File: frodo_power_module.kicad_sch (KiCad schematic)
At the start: 75 parts, among them J1 Keystone 1098, J10 SWD Header, J2 Molex MicroFit 2x2, J3 Molex MicroFit 2x2, J4 Molex MicroFit 2x2, J5 Molex MicroFit 2x2, J6 Molex MicroFit 2x2, J7 JST-GH, J8 JST-GH, J9 JST-GH, U1 STM32F042F6Px, U2 L7805, U3 AZ1117I-3.3, U4 BQ25171-Q1, U5 BQ29200, U6 MCP2562-E-SN, U7 INA213, Y1 8MHz

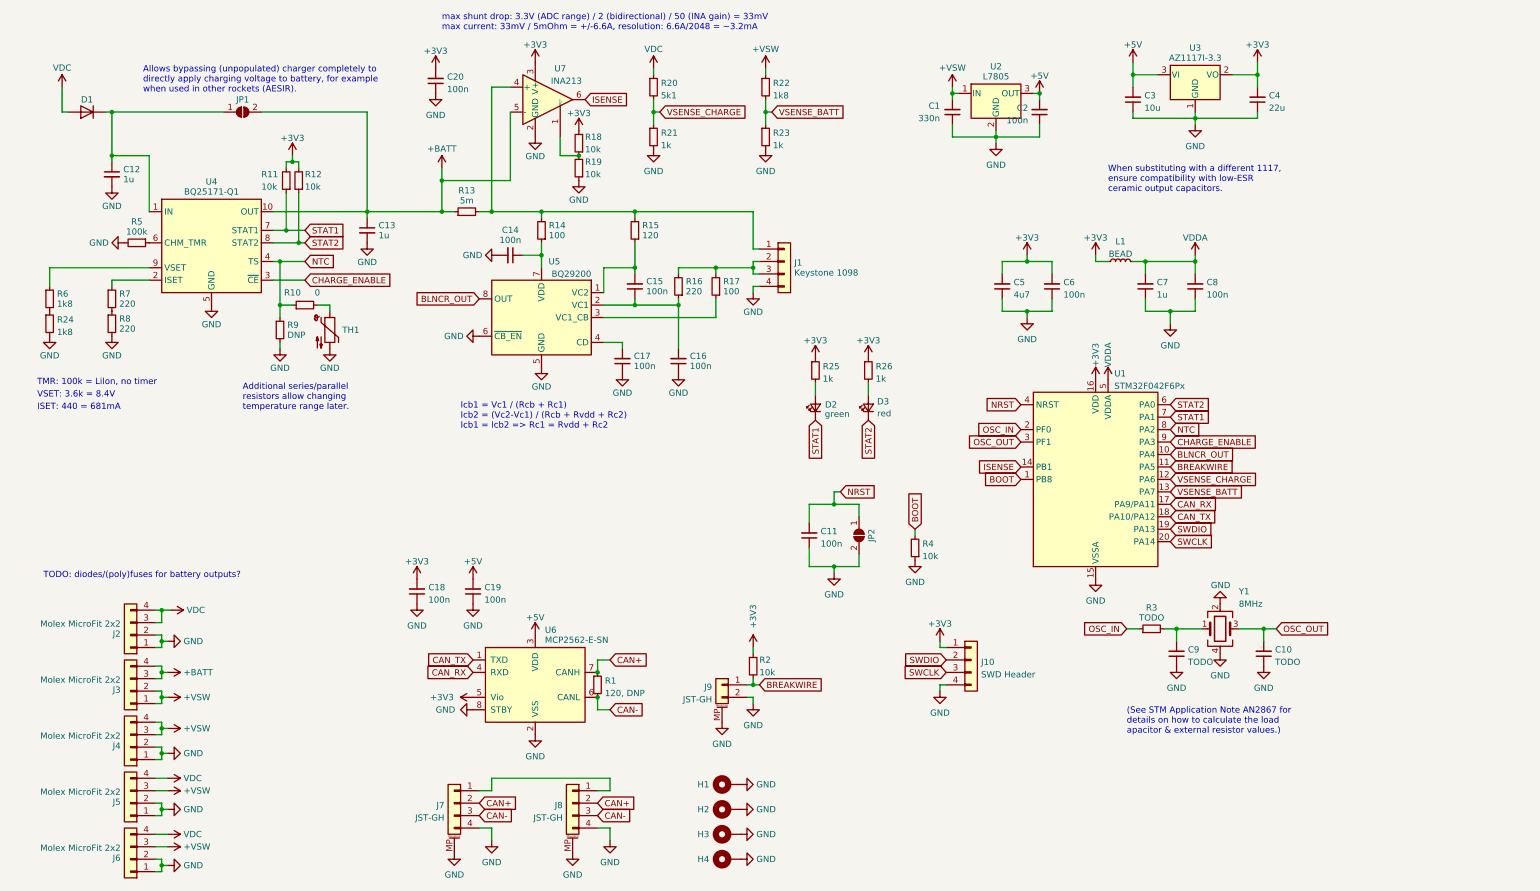
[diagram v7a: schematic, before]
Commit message: Add fuses to outputs, finish BOM
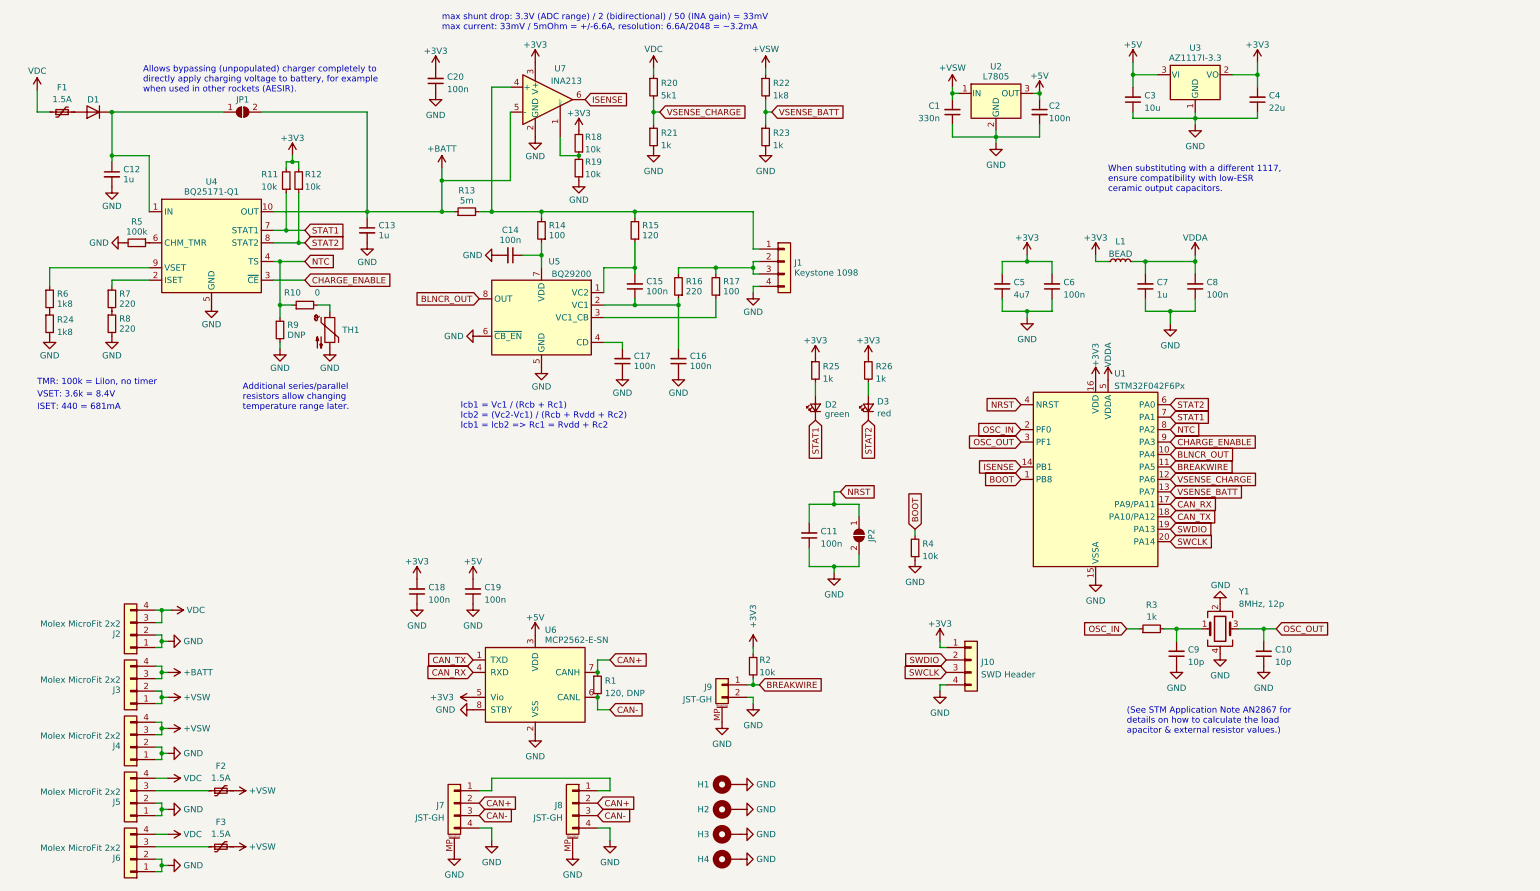
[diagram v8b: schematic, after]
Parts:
- added F1, F2, F3: 1.5A, Fuse:Fuse_1206_3216Metric, symbol Device:Polyfuse_Small
- C10, C9: value TODO -> 10p; LCSC# C1653 -> C1634; Part# CL10C220JB8NNNC -> CL10C100JB8NNNC
- D1: Manufacturer (none) -> Micro Commercial Co; Part# (none) -> SK34A-LTP
- H1, H2, H3, H4, J10, JP1, JP2, R9: DigiKey# (none) -> N/A; LCSC# (none) -> N/A; Manufacturer (none) -> N/A; Part# (none) -> N/A
- J1: DigiKey# (none) -> 36-1098-ND; Manufacturer (none) -> Keystone Electronics; Part# (none) -> 1098
- J2, J3, J4, J5, J6: LCSC# (none) -> C122413; Manufacturer (none) -> MOLEX; Part# (none) -> 0430450400
- J9: LCSC# (none) -> C189893; Manufacturer (none) -> JST
- R10: LCSC# (none) -> C100044; Part# (none) -> RC0603FR-070RL
- R13: LCSC# C105881 -> C723630; Part# RC0603FR-07330RL -> PA2512FKE7W0R005E
- R14, R17: LCSC# (none) -> C105588; Part# (none) -> RC0603FR-07100RL
- R16, R7, R8: LCSC# C98220 -> C107696; Part# RC0603FR-0710KL -> RC0603FR-07220RL
- R20: LCSC# C185354 -> C105580; Part# RC0603FR-071K8L -> RC0603FR-075K1L
- R3: value TODO -> 1k; LCSC# C105881 -> C22548; Part# RC0603FR-07330RL -> RC0603FR-071KL
- R5: LCSC# C98220 -> C14675; Part# RC0603FR-0710KL -> RC0603FR-07100KL
- U1: DigiKey# (none) -> 497-19656-1-ND; Manufacturer (none) -> STMicroelectronics; Part# (none) -> STM32F042F6P6TR
- U4: DigiKey# (none) -> 296-BQ25171QWDRCRQ1CT-ND; Manufacturer (none) -> Texas Instruments; Part# (none) -> BQ25171QWDRCRQ1
- U5: DigiKey# (none) -> 296-32038-1-ND; Manufacturer (none) -> Texas Instruments; Part# (none) -> BQ29200DRBT
- U7: DigiKey# (none) -> 296-26072-1-ND; Manufacturer (none) -> Texas Instruments; Part# (none) -> INA213AIDCKR
- Y1: value 8MHz -> 8MHz, 12p; DigiKey# (none) -> 50-ECS-80-12-33-JGN-CT-ND; Manufacturer Seiko Epson -> ECS Inc.; Part# (none) -> ECS-80-12-33-JGN-TR
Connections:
- net +5V: now also C2.1; no longer C2.2
- net +VSW: now also F2.2, F3.2; no longer J5.3 (Pin_3), J6.3 (Pin_3)
- net GND: now also C2.2; no longer C2.1
- net VDC: now also F1.1; no longer D1.2 (A)
- new net: D1.2 (A), F1.2
- new net: F3.1, J6.3 (Pin_3)
- new net: F2.1, J5.3 (Pin_3)
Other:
- note removed: "TODO: diodes/(poly)fuses for battery outputs?"
- moved on the sheet: D1
